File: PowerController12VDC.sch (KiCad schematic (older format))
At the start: 0 parts

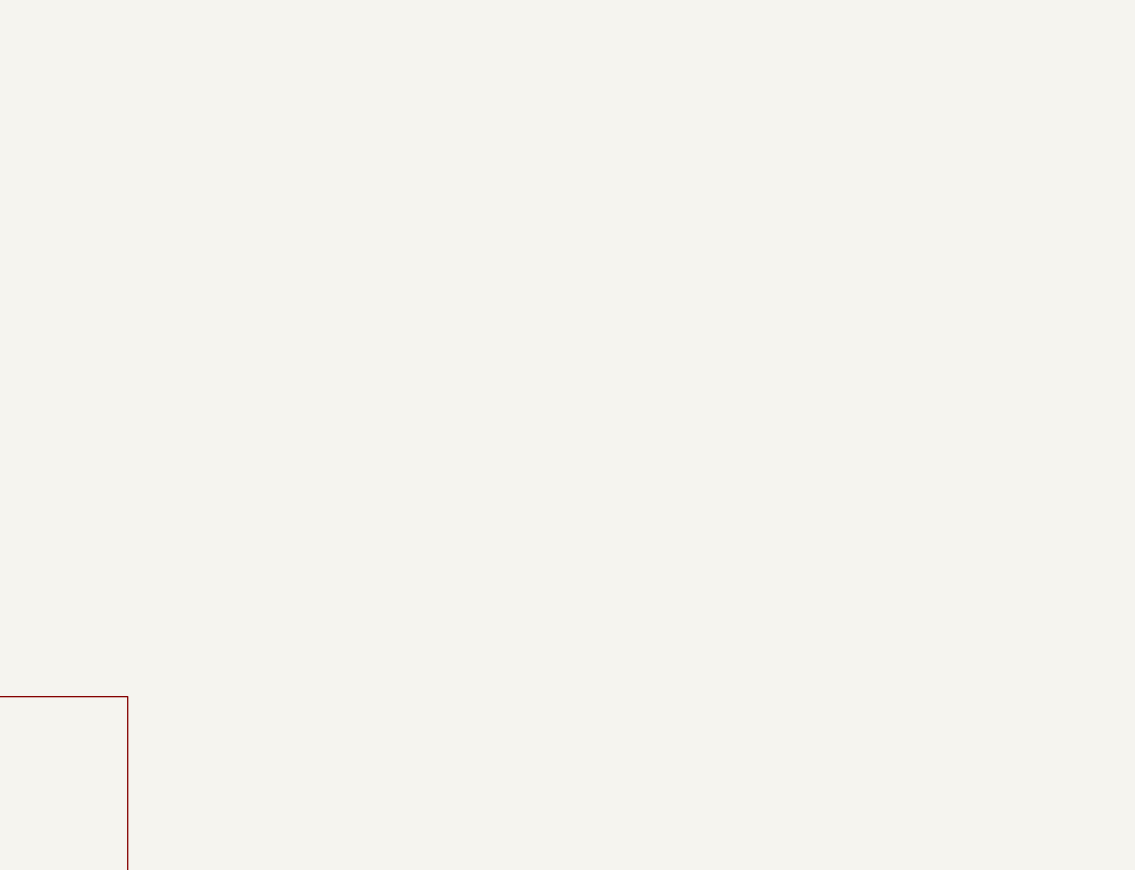
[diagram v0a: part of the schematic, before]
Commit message: Change PS to SMPS 5v, LDO 3.3V
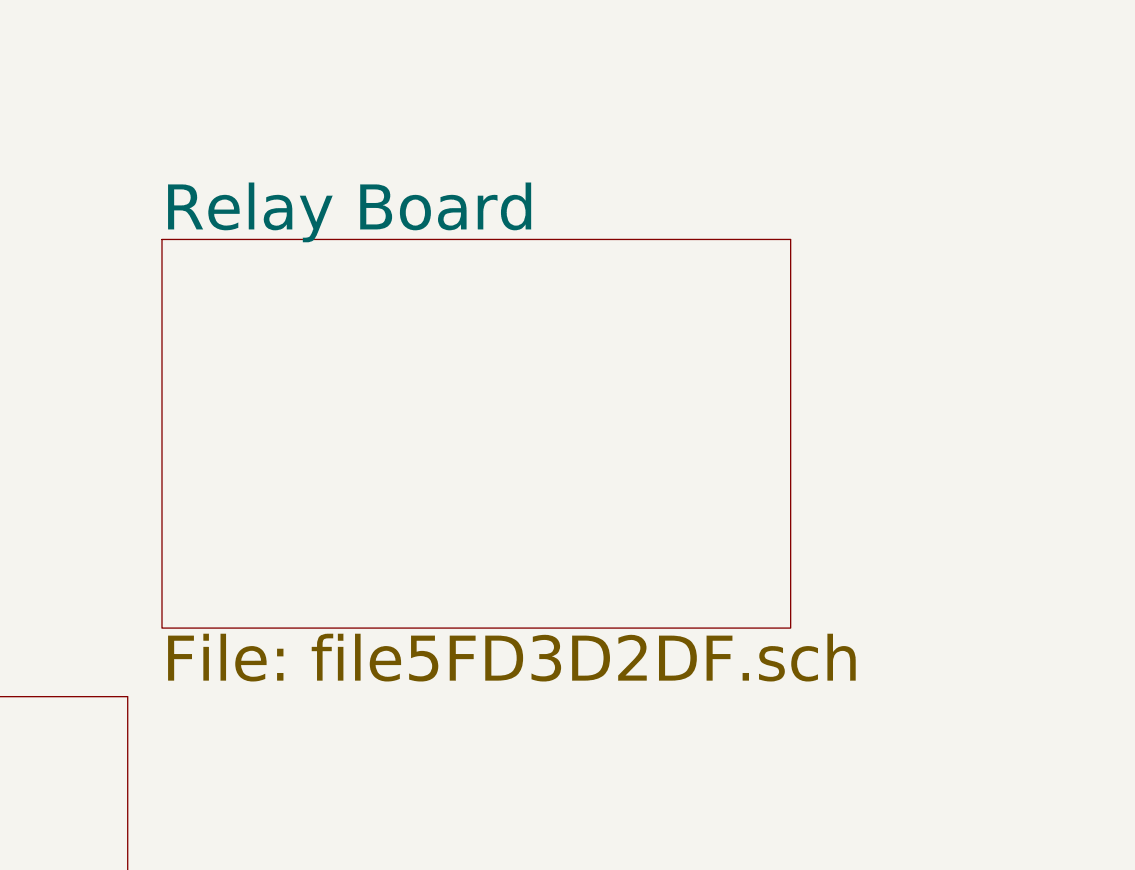
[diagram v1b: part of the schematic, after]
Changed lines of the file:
@@
 $Descr USLedger 17000 11000
 encoding utf-8
-Sheet 1 5
+Sheet 1 6
 Title "KQ9P Power Controller 12VDC"
 Date "2020-12-08"
@@
 F1 "file5FD26A29.sch" 50
 $EndSheet
+$Sheet
+S 6250 5400 2750 1700
+U 5FD3D2E0
+F0 "Relay Board" 197
+F1 "file5FD3D2DF.sch" 197
+$EndSheet
 $EndSCHEMATC
